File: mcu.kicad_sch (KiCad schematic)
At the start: 5 parts, among them J2 Interface, U1 ESP32-S3-WROOM-2

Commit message: Routed RF Core
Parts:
- removed J2: Interface, symbol Connector_Generic:Conn_02x20_Top_Bottom
- added AE1: GNSS, Connector_Coaxial:U.FL_Molex_MCRF_73412-0110_Vertical, symbol Device:Antenna_Shield
- added AE6: SMA, Connector_Coaxial:SMA_Amphenol_132289_EdgeMount, symbol Device:Antenna_Shield
- added C100, C104, C106, C109, C113, C99: 100pF, Capacitor_SMD:C_0603_1608Metric, symbol Device:C_Small
- added C101, C102, C103, C112: 1nF, Capacitor_SMD:C_0402_1005Metric, symbol Device:C_Small
- added C105, C107, C110, C114, C16, C37, C38: 0.1uF, Capacitor_SMD:C_0603_1608Metric, symbol Device:C_Small
- added C108, C111: 1nF, Capacitor_SMD:C_0603_1608Metric, symbol Device:C_Small
- added C17, C36, C39, C87: 4.7uF, Capacitor_SMD:C_0603_1608Metric, symbol Device:C_Small
- added C23, C25, C28, C40, C7, C96: 10uF, Capacitor_SMD:C_0603_1608Metric, symbol Device:C_Small
- added C24, C29, C3, C6, C8, C89, C90, C91, C92, C95: 100nF, Capacitor_SMD:C_0603_1608Metric, symbol Device:C_Small
- added C26, C27, C93: 1uF, Capacitor_SMD:C_0603_1608Metric, symbol Device:C_Small
- added C5: 47uF, Capacitor_SMD:C_0805_2012Metric, symbol Device:C_Small
- added FB1, FB2: FerriteBead, Inductor_SMD:L_0805_2012Metric, symbol Device:FerriteBead
- added IC1: SKY13373-460LF, PTCR:QFN50P200X200X60-13N-D, symbol PTCR-V5:SKY13373-460LF
- added IC2, IC3: AD8318ACPZ-REEL7, PTCR:QFN65P400X400X100-17N, symbol PTCR-V5:AD8318ACPZ-REEL7
- added J1: Interface, Connector_PinHeader_2.54mm:PinHeader_2x20_P2.54mm_Vertical, symbol Connector_Generic:Conn_02x20_Odd_Even
- added J4: BUTTON, Connector_PinHeader_1.27mm:PinHeader_1x02_P1.27mm_Vertical, symbol Connector:Conn_01x02_Socket
- added J6: ROTARY_ENCODER, Connector_PinHeader_1.27mm:PinHeader_1x03_P1.27mm_Vertical, symbol Connector:Conn_01x03_Socket
- added L2: 27nH, symbol Device:L
- added M1: Motor_DC, Connector_PinHeader_1.27mm:PinHeader_1x02_P1.27mm_Vertical, symbol Motor:Motor_DC
- added R70, R74, R76, R78, R79, R80, R95: 10K, Resistor_SMD:R_0603_1608Metric, symbol Device:R_Small_US
- added R75: 2.2K, Resistor_SMD:R_0603_1608Metric, symbol Device:R_Small_US
- added R77: 100K, Resistor_SMD:R_0603_1608Metric, symbol Device:R_Small_US
- added R83, R84, R86, R87: 96.2R, Resistor_SMD:R_0402_1005Metric, symbol Device:R_Small_US
- added R85, R88: 71.5R, Resistor_SMD:R_0402_1005Metric, symbol Device:R_Small_US
- added R89, R93: 52.3R, Resistor_SMD:R_0402_1005Metric, symbol Device:R_Small_US
- added R90, R94: 499R, Resistor_SMD:R_0402_1005Metric, symbol Device:R_Small_US
- added R91, R92: 10K, Resistor_SMD:R_0402_1005Metric, symbol Device:R_Small_US
- added R96, R97: 1K, Resistor_SMD:R_0402_1005Metric, symbol Device:R_Small_US
- added TP2: +3V3_NSY, TestPoint:TestPoint_Pad_D1.0mm, symbol Connector:TestPoint
- added TP4: +3V3_GNSS, TestPoint:TestPoint_Pad_D1.0mm, symbol Connector:TestPoint
- added U10: DRV2605LDGS, Package_SO:TSSOP-10_3x3mm_P0.5mm, symbol Driver:DRV2605LDGS
- added U11: LC76G, PTCR:XCVR_LC76G, symbol PTCR-V5:LC76G
- added U13: SA818S, PTCR:XCVR_SA818S, symbol PTCR-V5:SA818S
- added U2: TCD-10-23BDX+, PTCR:TCD-10-23BDX+, symbol PTCR-V5:TCD-10-23BDX+
- added U21: WM8960, PTCR:QFN-32, symbol PTCR-V5:WM8960
- added U23: E22-900M30S, PTCR:XCVR_E22-900M30S, symbol PTCR-V5:E22-900M30S
- added U24: E22-170M30S, PTCR:XCVR_E22-900M30S, symbol PTCR-V5:E22-900M30S
- added U3: MCP23017x-x-ML, Package_DFN_QFN:QFN-28-1EP_6x6mm_P0.65mm_EP4.25x4.25mm, symbol Interface_Expansion:MCP23017x-x-ML
- added U4: BMP390, PTCR:10LGA_2X2X0p75_BOS, symbol PTCR-LIB:BMP390
- added U6: LSM6DSOXTR, PTCR:LGA-14L_STM, symbol PTCR-LIB:LSM6DSOXTR
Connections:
- net +3V3: now also C104.1, C105.1, C106.2, C107.2, C109.1, C110.1, C113.2, C114.2, C23.1, C24.1, C29.1, C40.1, C8.1, C95.1, C96.1, FB1.1, FB2.2, IC1.6 (VDD), IC2.3 (VPSI_2), IC2.4 (VPSI), IC2.9 (VPSO), IC3.3 (VPSI_2), IC3.4 (VPSI), IC3.9 (VPSO), J1.18 (Pin_18), J1.2 (Pin_2), R78.1, R79.1, R80.1, R91.2, R92.2, R95.2, U13.8 (VBAT), U23.10 (VIN), U23.9 (VIN), U24.10 (VIN), U24.9 (VIN), U3.5 (V_{DD}), U4.1 (VDDIO), U4.10 (VDD), U4.6 (CSB), U6.12 (CS), U6.5 (VDDIO), U6.8 (VDD)
- net +5V: now also J1.1 (Pin_1), J1.3 (Pin_3)
- net BUSY_170: now also U1.5 (IO5), U24.14 (BUSY); no longer U1.13 (USB_D-/IO19)
- net BUSY_900: now also U23.14 (BUSY)
- net BUTTON0: now also J4.2 (Pin_2), U3.17 (GPA0); no longer U1.15 (IO3)
- net BUTTON1: now also U3.18 (GPA1); no longer U1.4 (IO4)
- net CLK: now also U11.25 (SPI_CLK), U23.18 (SCK), U24.18 (SCK)
- net CS_170: now also U24.19 (NSS)
- net CS_900: now also U23.19 (NSS)
- net DIO1_170: now also U24.13 (DIO1)
- net DIO1_900: now also U23.13 (DIO1)
- net GND: now also AE1.2 (Shield), AE6.2 (Shield), C100.1, C103.1, C104.2, C105.2, C106.1, C107.1, C108.2, C109.2, C110.2, C111.2, C112.1, C113.1, C114.1, C16.2, C17.2, C23.2, C24.2, C25.2, C26.1, C27.1, C28.2, C29.2, C3.1, C36.2, C37.2, C38.2, C39.2, C40.2, C5.1, C6.1, C7.1, C8.2, C87.2, C89.1, C95.2, C96.2, C99.2, IC1.10 (GND_4), IC1.12 (GND_5), IC1.13 (EPAD), IC1.2 (GND_1), IC1.7 (GND_2), IC1.8 (GND_3), IC2.1 (CMIP_2), IC2.11 (CMIP_4), IC2.12 (CMIP), IC2.17 (EP), IC2.2 (CMIP_3), IC2.8 (CMOP), IC3.1 (CMIP_2), IC3.11 (CMIP_4), IC3.12 (CMIP), IC3.17 (EP), IC3.2 (CMIP_3), IC3.8 (CMOP), J1.10 (Pin_10), J1.13 (Pin_13), J1.19 (Pin_19), J1.26 (Pin_26), J1.29 (Pin_29), J1.33 (Pin_33), J1.40 (Pin_40), J1.5 (Pin_5), J4.1 (Pin_1), J6.3 (Pin_3), R74.2, R76.2, R77.1, R83.2, R84.2, R86.1, R87.1, R89.1, R90.2, R93.1, R94.2, U10.4 (IN/TRIG), U10.8 (GND), U11.1 (GND), U11.10 (GND), U11.12 (GND), U11.28 (GND), U13.10 (GND), U13.9 (GND), U2.2 (GND), U2.5 (NC), U21.20 (SPKGND2), U21.24 (SPKGND1), U21.28 (AGND), U21.9 (DGND), U21.PADDLE (GNDPADDLE), U23.1 (GND), U23.11 (GND), U23.12 (GND), U23.2 (GND), U23.20 (GND), U23.22 (GND), U23.3 (GND), U23.4 (GND), U23.5 (GND), U24.1 (GND), U24.11 (GND), U24.12 (GND), U24.2 (GND), U24.20 (GND), U24.22 (GND), U24.3 (GND), U24.4 (GND), U24.5 (GND), U3.11 (A0), U3.12 (A1), U3.13 (A2), U3.29 (EP), U3.6 (V_{SS}), U4.3 (VSS), U4.5 (SDO), U4.8 (VSS), U4.9 (VSS), U6.1 (SDO/SA0), U6.2 (SDX), U6.3 (SCX), U6.6 (GND), U6.7 (GND)
- net H/L: now also R80.2, U13.7 (H/L), U3.21 (GPA4); no longer U1.35 (MTMS/IO42)
- net MISO: now also U11.26 (SPI_MISO), U23.17 (MOSI), U24.17 (MOSI)
- net MOSI: now also U11.27 (SPI_MOSI), U23.16 (MISO), U24.16 (MISO)
- net MOTOR: now also U10.5 (EN), U3.1 (GPB4)
- net NRST_RADIO: now also C25.1, C28.1, U23.15 (~{RST}), U24.15 (~{RST}), U3.3 (GPB6); no longer U1.14 (USB_D+/IO20)
- net PD: now also R79.2, U13.6 (PD), U3.20 (GPA3); no longer U1.34 (MTDI/IO41)
- net PTT: now also U1.19 (IO11), R78.2, U13.5 (PTT); no longer U1.33 (MTDO/IO40)
- net ROT_ENC1: now also J6.2 (Pin_2)
- net ROT_ENC2: now also J6.1 (Pin_1)
- net RXEN_170: now also U24.6 (RXEN), U3.2 (GPB5); no longer U1.19 (IO11)
- net RXEN_900: now also U23.6 (RXEN), U3.4 (GPB7); no longer U1.5 (IO5)
- net S3_BOOT: now also J1.38 (Pin_38)
- net S3_EN: now also J1.36 (Pin_36)
- net S3_IRQ: now also J1.34 (Pin_34)
- net S3_RXD0: now also J1.15 (Pin_15)
- net S3_TXD0: now also J1.17 (Pin_17)
- net SA818S_RXD: now also U13.16 (RXD)
- net SA818S_TXD: now also U13.17 (TXD)
- net SCL: now also J1.6 (Pin_6), U10.2 (SCL), U11.17 (I2C_SCL), U21.17 (SCL), U3.8 (SCK), U4.2 (SCK), U6.13 (SCL)
- net SDA: now also J1.4 (Pin_4), U10.3 (SDA), U11.16 (I2C_SDA), U21.18 (SDA), U3.9 (SDA), U4.4 (SDI), U6.14 (SDA)
- net SPI_CLK: now also J1.35 (Pin_35)
- net SPI_CS: now also J1.32 (Pin_32)
- net SPI_MISO: now also J1.39 (Pin_39)
- net SPI_MOSI: now also J1.37 (Pin_37)
- net WM8960_ACDDAT: now also J1.24 (Pin_24), U21.16 (ADCDAT)
- net WM8960_BLCK: now also J1.16 (Pin_16), U21.12 (BCLK)
- net WM8960_DACDAT: now also J1.22 (Pin_22), U21.14 (DACDAT)
- net WM8960_DAC/ADC_LRC: now also J1.20 (Pin_20), U21.13 (DACLRC), U21.15 (ADCLRC/GPIO)
- net WM8960_MLCK: now also J1.31 (Pin_31), U21.11 (MCLK)
- new net: C111.1, IC3.5 (CLPF)
- new net: C91.2, U21.29 (HEADPHONE_R)
- new net: C92.2, U21.31 (HEADPHONE_L)
- new net: R75.2, U21.1 (MICBIAS)
- new net: C37.1, U21.10 (DBVDD)
- new net: C17.1, U21.21 (SPKVDD2)
- new net: C36.1, U21.26 (SPKVDD1)
- new net: C39.1, U21.27 (VMID)
- new net: C90.2, U21.3 (LINPUT2)
- new net: R70.1, U21.30 (MONO_OUT)
- new net: C16.1, U21.32 (AVDD)
- new net: C93.2, U21.4 (LINPUT1)
- new net: C38.1, U21.8 (DCVDD)
- new net: L2.1, U11.14 (VDD_RF)
- new net: IC2.6 (VOUT), IC2.7 (VSET), R96.2
- new net: IC3.10 (TADJ), R94.1
- new net: C102.2, IC3.14 (INHI)
- new net: C112.2, IC3.15 (INLO)
- new net: IC3.6 (VOUT), IC3.7 (VSET), R97.2
- new net: C103.2, IC2.15 (INLO)
- new net: U13.11 (NC), U13.13 (NC), U13.14 (NC), U13.15 (NC), U13.2 (NC), U13.4 (NC)
- new net: C27.2, U10.1 (REG)
- new net: M1.1 (+), U10.7 (OUT+)
- new net: M1.2 (-), U10.9 (OUT-)
- new net: IC2.10 (TADJ), R90.1
- new net: U23.7 (TXEN), U23.8 (DIO2)
- new net: U24.7 (TXEN), U24.8 (DIO2)
- new net: U11.15 (RESERVED), U11.18 (RESERVED), U11.19 (RESERVED), U11.7 (RESERVED)
- new net: C108.1, IC2.5 (CLPF)
- new net: C101.2, IC2.14 (INHI)
- new net +3V3_GNSS: C6.2, C7.2, FB2.1, TP4.1, U11.8 (VCC)
- new net +3V3_NSY: C3.2, C5.2, FB1.2, TP2.1
- new net +BATT: C26.2, U10.10 (VDD)
- new net AD8318_EN: IC2.16 (ENBL), IC3.16 (ENBL), R91.1, R92.1
- new net ANT: AE6.1 (A), U2.4 (OUTPUT)
- new net AUDIO_ON: U13.1 (AUDIO_ON)
- new net CS_GNSS: U11.20 (SPI_CS)
- new net FWD: R96.1, U1.4 (IO4)
- new net FWD_IN: R83.1, R85.1, U2.1 (FWD)
- new net FWD_OUT: C101.1, R84.1, R85.2, R89.2
- new net FWD_TEMP: IC2.13 (TEMP)
- new net G_RESET: U11.9 (~{RESET})
- new net HP_L: C92.1
- new net HP_R: C91.1
- new net INT1_IMU: U6.4 (INT1)
- new net INTA_MCP: J1.14 (Pin_14), U3.16 (INTA)
- new net LINPUT1: C93.1, R77.2, U13.3 (AF_OUT)
- new net MIC_HS: C87.1, C90.1, R75.1, R76.1
- new net MONO_OUT: C89.2, R70.2, R74.1, U13.18 (MIC_IN)
- new net RESET_MCP: J1.8 (Pin_8), R95.1, U3.14 (~{RESET})
- new net REV: R97.1, U1.15 (IO3)
- new net REV_IN: R86.2, R88.1, U2.6 (REV)
- new net REV_OUT: C102.1, R87.2, R88.2, R93.2
- new net REV_TEMP: IC3.13 (TEMP)
- new net RF1: IC1.1 (J1), U13.12 (ANT)
- new net RF2: IC1.9 (J2), U23.21 (ANT)
- new net RF3: IC1.3 (J3), U24.21 (ANT)
- new net RFS_V1: C99.1, IC1.4 (V1)
- new net RFS_V2: C100.2, IC1.5 (V2)
- new net RF_IN: AE1.1 (A), L2.2, U11.11 (RF_IN)
- new net ROS: IC1.11 (RFC), U2.3 (INPUT)
- new net RXD1: U11.3 (RXD)
- new net TXD1: U11.2 (TXD)
- no-connect marks 0 -> 21
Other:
- note added: "Address: 0x6A"
- note added: "Address: 0x76"
- note added: "Antenna"
- note added: "Attenuator"
- note added: "Bidirectional Coupler"
- note added: "GNSS"
- note added: "Logarithmic Detector"
- note added: "Main"
- note added: "Switch RF"
- note removed: "MCU"
- moved on the sheet: C4, U1

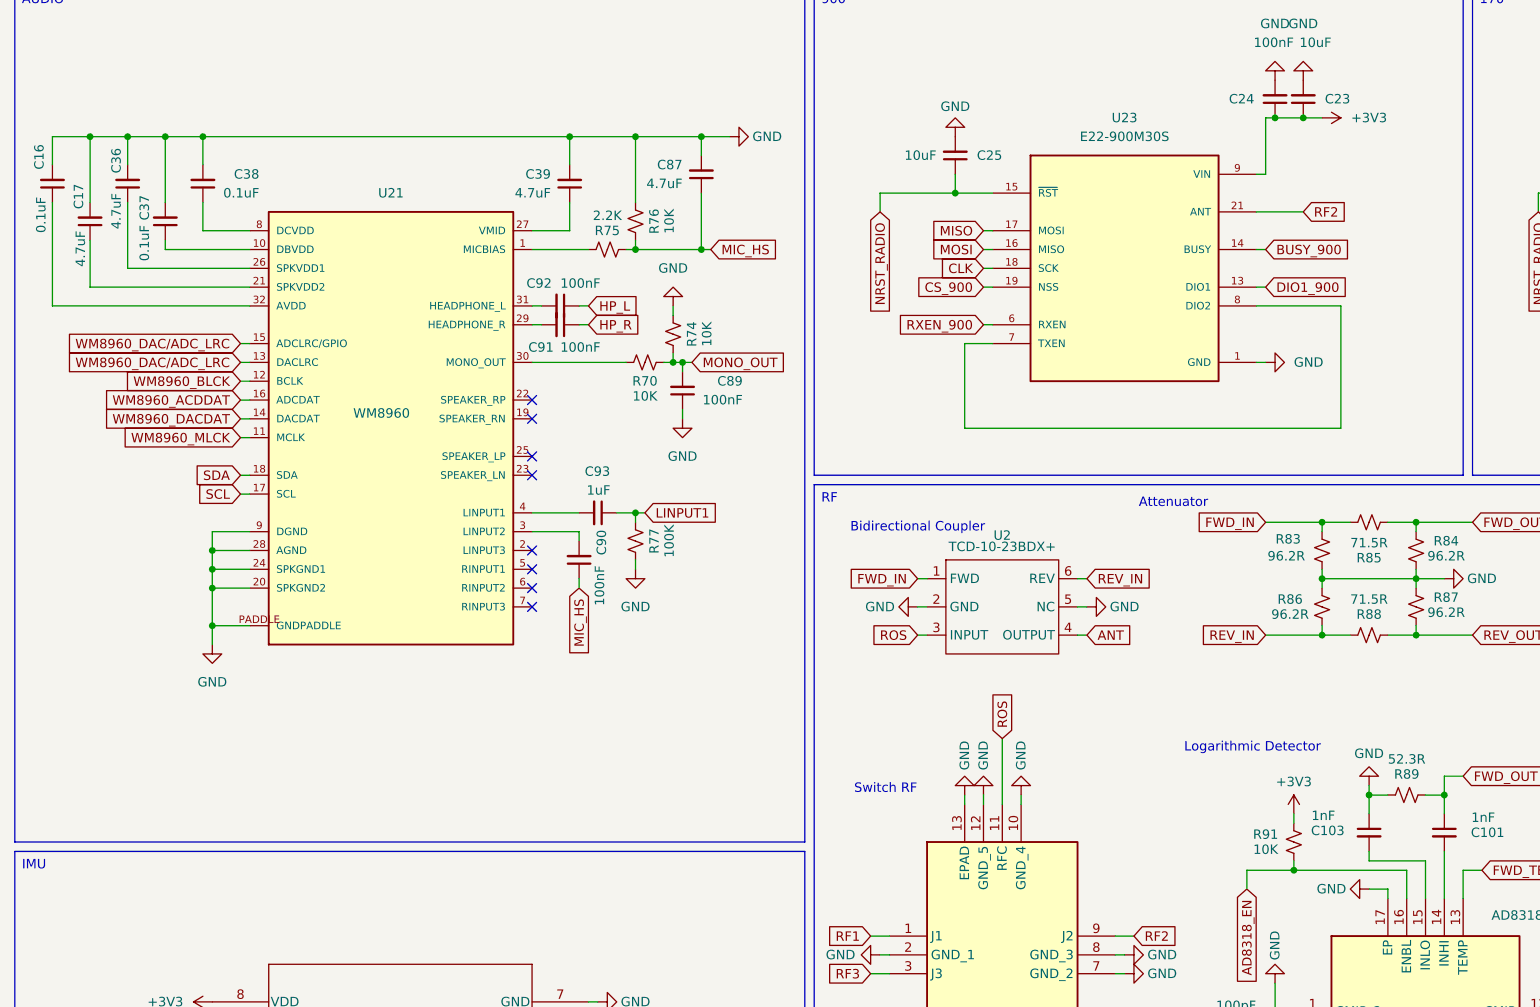
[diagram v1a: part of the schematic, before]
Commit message: Routed RF part and started routing MCU, SPI Bus, and other
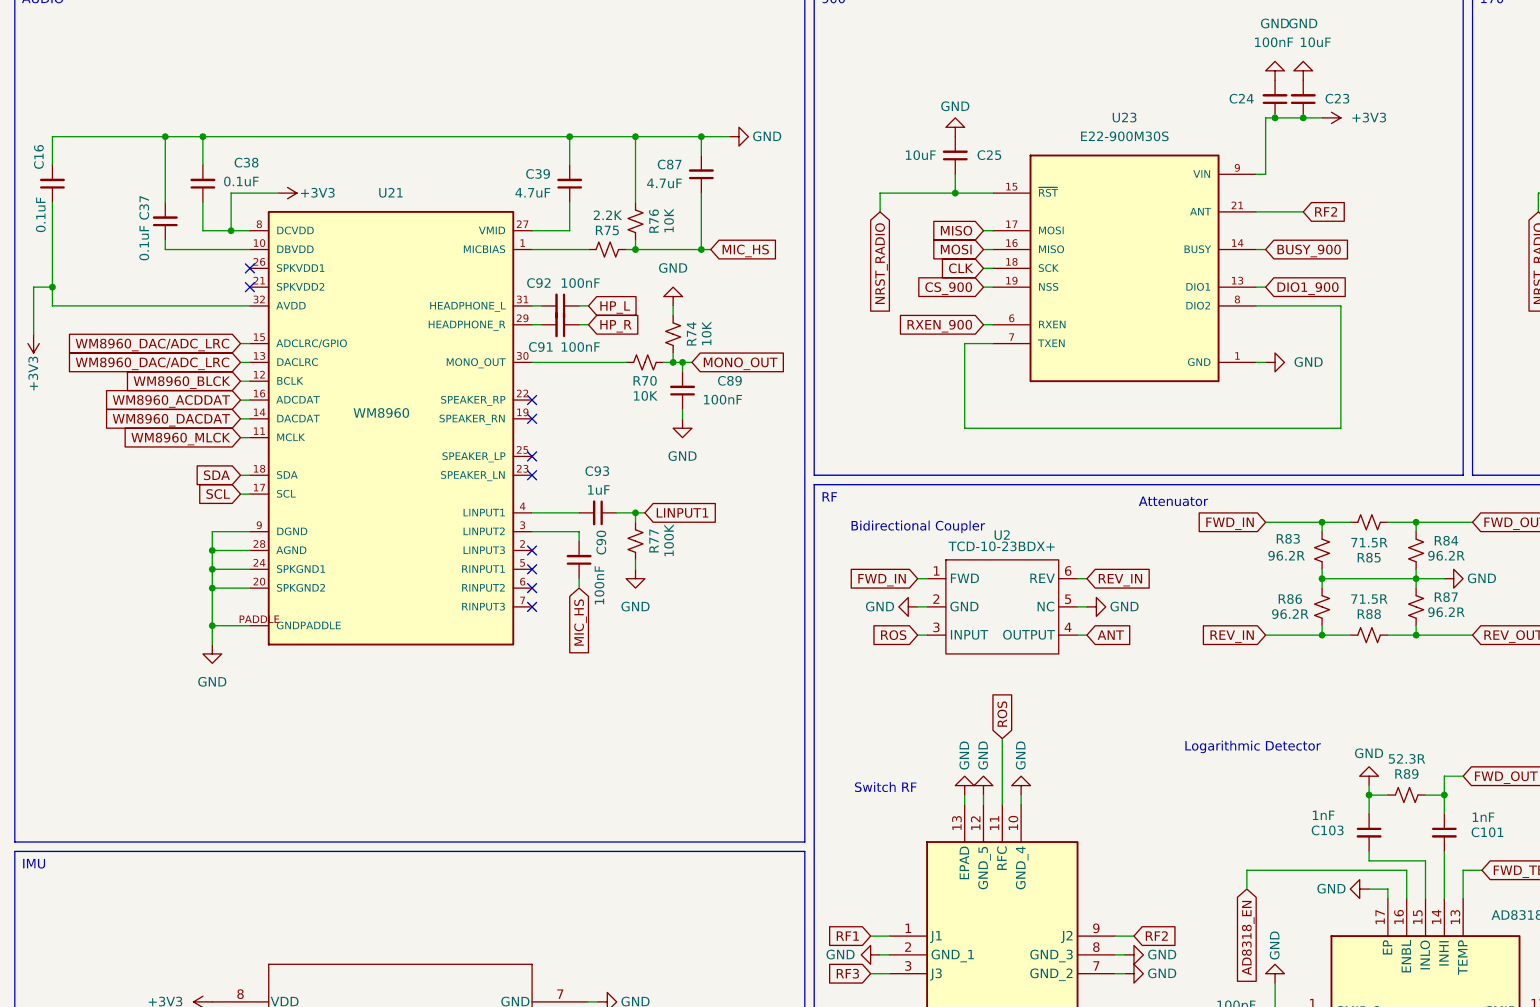
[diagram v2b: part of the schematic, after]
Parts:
- removed C17, C36: 4.7uF, Capacitor_SMD:C_0603_1608Metric, symbol Device:C_Small
- removed R91: 10K, Resistor_SMD:R_0402_1005Metric, symbol Device:R_Small_US
- C104, C105, C106, C107, C108, C109, C110, C111, C113, C114: footprint Capacitor_SMD:C_0603_1608Metric -> Capacitor_SMD:C_0402_1005Metric
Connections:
- net +3V3: now also C16.1, C38.1, U21.32 (AVDD), U21.8 (DCVDD)
- no-connect marks 21 -> 23

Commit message: Modified schematic to add dual battery with dual charger, dual gauge and power mux
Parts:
- removed J4: BUTTON, Connector_PinHeader_1.27mm:PinHeader_1x02_P1.27mm_Vertical, symbol Connector:Conn_01x02_Socket
- removed J6: ROTARY_ENCODER, Connector_PinHeader_1.27mm:PinHeader_1x03_P1.27mm_Vertical, symbol Connector:Conn_01x03_Socket
- added BT1: MAIN, Connector_JST:JST_EH_S2B-EH_1x02_P2.50mm_Horizontal, symbol Device:Battery_Cell
- added BT2: SECOND, Connector_JST:JST_EH_S2B-EH_1x02_P2.50mm_Horizontal, symbol Device:Battery_Cell
- added C10, C14: 100pF, Capacitor_SMD:C_0402_1005Metric, symbol Device:C_Small
- added C11, C12: NC, Capacitor_SMD:C_0402_1005Metric, symbol Device:C_Small
- added C115, C119, C120, C97: 4.7uF, Capacitor_SMD:C_0603_1608Metric, symbol Device:C_Small
- added C116, C117, C118, C30, C98: 1uF, Capacitor_SMD:C_0402_1005Metric, symbol Device:C_Small
- added C121, C13, C9: 100nF, Capacitor_SMD:C_0402_1005Metric, symbol Device:C_Small
- added C31, C94: 0.1uF, Capacitor_SMD:C_0402_1005Metric, symbol Device:C_Small
- added D7: D_TVS, symbol Device:D_TVS
- added FB3: 600R @100MHz 500mA, Inductor_SMD:L_0402_1005Metric, symbol Device:FerriteBead
- added FB4: 600R @100MHz 1.5A, Inductor_SMD:L_0603_1608Metric, symbol Device:FerriteBead
- added IC4: TPS2121RUXT, PTCR:TPS2121RUXT, symbol PTCR-V5:TPS2121RUXT
- added IC5, IC6: MAX17048G+T10, SON50P200X200X80-9N-D, symbol PTCR-V5:MAX17048G+T10
- added IC7: TCA9543ADR, SOIC127P600X175-14N, symbol PTCR-V5:TCA9543ADR
- added J2: Connector, Connector_FFC-FPC:Amphenol_F32R-1A7x1-11029_1x29-1MP_P0.5mm_Horizontal, symbol Connector_Generic:Conn_02x15_Counter_Clockwise
- added J4: JST_MAIN, Connector_JST:JST_EH_S2B-EH_1x02_P2.50mm_Horizontal, symbol Connector_Generic:Conn_01x02
- added R100: 13.7K, Resistor_SMD:R_0402_1005Metric, symbol Device:R_Small_US
- added R101: 23.7K, Resistor_SMD:R_0402_1005Metric, symbol Device:R_Small_US
- added R102, R103, R106: 5K, Resistor_SMD:R_0402_1005Metric, symbol Device:R_Small_US
- added R104: 51.1K, Resistor_SMD:R_0402_1005Metric, symbol Device:R_Small_US
- added R105: 10.2K, Resistor_SMD:R_0402_1005Metric, symbol Device:R_Small_US
- added R107, R108, R114, R115: 1K, Resistor_SMD:R_0402_1005Metric, symbol Device:R_Small_US
- added R109, R116, R117, R118, R119, R120, R121, R122, R123, R124, R98, R99: 10K, Resistor_SMD:R_0402_1005Metric, symbol Device:R_Small_US
- added R110, R113: 1.13K, Resistor_SMD:R_0402_1005Metric, symbol Device:R_Small_US
- added R111, R112: 1.18K, Resistor_SMD:R_0402_1005Metric, symbol Device:R_Small_US
- added R125: 0R, Resistor_SMD:R_0402_1005Metric, symbol Device:R_Small_US
- added R126: 10R, Resistor_SMD:R_0402_1005Metric, symbol Device:R_Small_US
- added R91: 3.3K, Resistor_SMD:R_0402_1005Metric, symbol Device:R_Small_US
- added TP5, TP6: +3V3_RF, TestPoint:TestPoint_Pad_D1.0mm, symbol Connector:TestPoint
- added U5: IS31FL3218-QF, Package_DFN_QFN:QFN-24-1EP_4x4mm_P0.5mm_EP2.7x2.7mm, symbol Driver_LED:IS31FL3218-QF
- added U7, U9: BQ24075RGT, Package_DFN_QFN:VQFN-16-1EP_3x3mm_P0.5mm_EP1.6x1.6mm, symbol Battery_Management:BQ24075RGT
- added U8: MCP23017x-x-ML, Package_DFN_QFN:QFN-28-1EP_6x6mm_P0.65mm_EP4.25x4.25mm, symbol Interface_Expansion:MCP23017x-x-ML
- C100, C16, C24, C26, C27, C29, C3, C37, C38, C4, C6, C7, C8, C89, C90, C91, C92, C93, C95, C99: footprint Capacitor_SMD:C_0603_1608Metric -> Capacitor_SMD:C_0402_1005Metric
- FB1: value FerriteBead -> 600R @100MHz 1A; footprint Inductor_SMD:L_0805_2012Metric -> Inductor_SMD:L_0603_1608Metric
- FB2: value FerriteBead -> 600R @100MHz 500mA; footprint Inductor_SMD:L_0805_2012Metric -> Inductor_SMD:L_0402_1005Metric
- L2: value 27nH -> 68nH; footprint (none) -> Inductor_SMD:L_0402_1005Metric
- R70, R74, R75, R76, R77, R78, R79, R80, R81, R82, R95: footprint Resistor_SMD:R_0603_1608Metric -> Resistor_SMD:R_0402_1005Metric
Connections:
- net +BATT is gone; now on net +3V3: C26.2, U10.10 (VDD)
- net +3V3: now also C121.2, C30.1, C31.1, C9.1, FB3.2, FB4.2, IC7.14 (VCC), J2.1 (Pin_1), J2.2 (Pin_2), R117.2, R118.2, R119.2, R120.2, R121.2, R122.2, R123.2, R124.2, R98.2, U5.3 (VCC), U8.11 (A0), U8.5 (V_{DD}); no longer C104.1, C105.1, C106.2, C107.2, C109.1, C110.1, C113.2, C114.2, C23.1, C24.1, C29.1, C40.1, C95.1, C96.1, IC1.6 (VDD), IC2.3 (VPSI_2), IC2.4 (VPSI), IC2.9 (VPSO), IC3.3 (VPSI_2), IC3.4 (VPSI), IC3.9 (VPSO), R92.2, U13.8 (VBAT), U23.10 (VIN), U23.9 (VIN), U24.10 (VIN), U24.9 (VIN)
- net +3V3_GNSS: now also R99.2
- net +5V: now also C118.2, C98.2, U7.13 (IN), U9.13 (IN)
- net AD8318_EN: now also U3.28 (GPB3)
- net BUTTON0: now also J2.18 (Pin_18)
- net BUTTON1: now also J2.3 (Pin_3)
- net GND: now also BT1.2 (-), BT2.2 (-), C11.2, C115.1, C116.2, C117.2, C118.1, C119.2, C12.2, C120.1, C121.1, C13.2, C14.2, C30.2, C31.2, C9.2, C94.2, C97.2, C98.1, D7.1 (A1), IC4.12 (GND), IC5.1 (CTG), IC5.4 (GND), IC5.6 (QSTRT), IC5.9 (EP), IC6.1 (CTG), IC6.4 (GND), IC6.6 (QSTRT), IC6.9 (EP), IC7.1 (A0), IC7.2 (A1), IC7.7 (GND), J2.14 (Pin_14), J2.15 (Pin_15), J4.2 (Pin_2), R102.1, R103.2, R104.2, R106.1, R109.1, R110.1, R111.2, R112.2, R113.1, R116.1, R91.2, U5.25 (GND), U5.4 (GND), U7.14 (TMR), U7.15 (SYSOFF), U7.17 (VSS), U7.4 (~{CE}), U7.6 (EN1), U7.8 (VSS), U8.12 (A1), U8.13 (A2), U8.29 (EP), U8.6 (V_{SS}), U9.14 (TMR), U9.15 (SYSOFF), U9.17 (VSS), U9.4 (~{CE}), U9.6 (EN1), U9.8 (VSS)
- net INTA_MCP: now also U8.16 (INTA); no longer J1.14 (Pin_14)
- net JOYSTICK_X: now also J2.5 (Pin_5)
- net JOYSTICK_Y: now also J2.4 (Pin_4)
- net RESET_MCP: now also U8.14 (~{RESET})
- net RFS_V1: now also U3.23 (GPA6)
- net RFS_V2: now also U3.22 (GPA5)
- net RF_IN: now also C10.1, C12.1, R125.2; no longer AE1.1 (A), L2.2, U11.11 (RF_IN)
- net ROT_ENC1: now also J2.17 (Pin_17)
- net ROT_ENC2: now also J2.16 (Pin_16)
- net SCL: now also IC7.12 (SCL), J2.7 (Pin_7), U5.6 (SCL), U8.8 (SCK); no longer U11.17 (I2C_SCL)
- net SDA: now also IC7.13 (SDA), J2.6 (Pin_6), U5.5 (SDA), U8.9 (SDA); no longer U11.16 (I2C_SDA)
- net at L2.1: now also C13.1, C14.1, R126.1; no longer U11.14 (VDD_RF)
- net SDB: now reaches U3.19 (GPA2)
- net SDB: now also R98.1, U5.24 (~{SDB})
- net INTA_MCP_2: now reaches J1.11 (GPIO5)
- net at U11.24 (D_SEL): now also R99.1
- net BAT_OUT: now reaches U11.6 (V_BCKP)
- net BAT_OUT: now also IC4.1 (OUT_1), IC4.8 (OUT_2), J4.1 (Pin_1)
- new net: R109.2, U7.1 (TS)
- new net: R111.1, U7.12 (ILIM)
- new net: R110.2, U7.16 (ISET)
- new net: R107.2, U7.7 (~{PGOOD})
- new net: R108.1, U7.9 (~{CHG})
- new net: AE1.1 (A), C11.1, D7.2 (A2), L2.2, R125.1
- new net: R116.2, U9.1 (TS)
- new net: R112.1, U9.12 (ILIM)
- new net: R113.2, U9.16 (ISET)
- new net: R114.2, U9.7 (~{PGOOD})
- new net: R115.1, U9.9 (~{CHG})
- new net: IC4.5 (OV1), R101.2, R102.2
- new net: IC4.6 (PR1), R105.1, R106.2
- new net: C94.1, IC4.11 (SS)
- new net: IC4.4 (OV2), R100.2, R103.1
- new net: C10.2, U11.11 (RF_IN)
- new net: R91.1, U5.2 (R_EXT)
- new net: IC4.10 (ILIM), R104.1
- new net +3V3_RF: C104.1, C105.1, C106.2, C107.2, C109.1, C110.1, C113.2, C114.2, FB3.1, IC1.6 (VDD), IC2.3 (VPSI_2), IC2.4 (VPSI), IC2.9 (VPSO), IC3.3 (VPSI_2), IC3.4 (VPSI), IC3.9 (VPSO), R92.2, TP5.1
- new net BAT1: BT1.1 (+), C115.2, C116.1, IC5.2 (CELL), IC5.3 (VDD), U7.2 (BAT), U7.3 (BAT)
- new net BAT1_CHG: R108.2, U8.18 (GPA1)
- new net BAT1_INT: IC5.5 (~{ALRT}), IC7.4 (~{INT0}), R120.1
- new net BAT1_OUT: C97.1, IC4.7 (IN1), R101.1, R105.2, U7.10 (OUT), U7.11 (OUT), U7.5 (EN2)
- new net BAT1_PGOOD: R107.1, U8.17 (GPA0)
- new net BAT2: BT2.1 (+), C117.1, C120.2, IC6.2 (CELL), IC6.3 (VDD), U9.2 (BAT), U9.3 (BAT)
- new net BAT2_CHG: R115.2, U8.20 (GPA3)
- new net BAT2_INT: IC6.5 (~{ALRT}), IC7.8 (~{INT1}), R119.1
- new net BAT2_OUT: C119.1, IC4.2 (IN2), R100.1, U9.10 (OUT), U9.11 (OUT), U9.5 (EN2)
- new net BAT2_PGOOD: R114.1, U8.19 (GPA2)
- new net BATS_INT: IC7.11 (~{INT}), R124.1, U8.21 (GPA4)
- new net BATS_RESET: IC7.3 (~{RESET}), R123.1, U8.22 (GPA5)
- new net BAT_SEL: IC4.3 (CP2)
- new net BAT_VAL: IC4.9 (ST)
- new net D1B_A: J2.21 (Pin_21), U5.22 (OUT16)
- new net D1G_A: J2.20 (Pin_20), U5.23 (OUT17)
- new net D1R_A: J2.19 (Pin_19), U5.1 (OUT18)
- new net D2B_A: J2.24 (Pin_24), U5.19 (OUT13)
- new net D2G_A: J2.23 (Pin_23), U5.20 (OUT14)
- new net D2R_A: J2.22 (Pin_22), U5.21 (OUT15)
- new net D3B_A: J2.27 (Pin_27), U5.16 (OUT10)
- new net D3G_A: J2.26 (Pin_26), U5.17 (OUT11)
- new net D3R_A: J2.25 (Pin_25), U5.18 (OUT12)
- new net D4B_A: J2.30 (Pin_30), U5.13 (OUT7)
- new net D4G_A: J2.29 (Pin_29), U5.14 (OUT8)
- new net D4R_A: J2.28 (Pin_28), U5.15 (OUT9)
- new net D5B_A: J2.10 (Pin_10), U5.10 (OUT4)
- new net D5G_A: J2.9 (Pin_9), U5.11 (OUT5)
- new net D5R_A: J2.8 (Pin_8), U5.12 (OUT6)
- new net D6B_A: J2.13 (Pin_13), U5.7 (OUT1)
- new net D6G_A: J2.12 (Pin_12), U5.8 (OUT2)
- new net D6R_A: J2.11 (Pin_11), U5.9 (OUT3)
- new net INTA_MCP_1: J1.14 (GPIO4)
- new net SC0: IC5.8 (SDA), IC7.6 (SC0), R122.1
- new net SC1: IC6.8 (SDA), IC7.10 (SC1), R117.1
- new net SD0: IC5.7 (SCL), IC7.5 (SD0), R121.1
- new net SD1: IC6.7 (SCL), IC7.9 (SD1), R118.1
- new net VDD_RF: R126.2, U11.14 (VDD_RF)
- new net VIN: C23.1, C24.1, C29.1, C40.1, C95.1, C96.1, FB4.1, TP6.1, U13.8 (VBAT), U23.10 (VIN), U23.9 (VIN), U24.10 (VIN), U24.9 (VIN)
- no-connect marks 23 -> 29
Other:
- note added: "2 Channels I2C"
- note added: "BAT1 Charger"
- note added: "BAT1 Gauge"
- note added: "BAT2 Charger"
- note added: "BAT2 Gauge"
- note added: "Batteries"
- note added: "GNSS Antenna"
- note added: "GNSS Module"
- note added: "JST Connector"
- note added: "Power MUX"
- note added: "RF"
- note added: "Radio"
- moved on the sheet: AE1, AE6, C100, C101, C102, C103, C104, C105, C106, C107, C108, C109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
